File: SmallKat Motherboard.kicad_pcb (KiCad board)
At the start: 2 copper layers, 100 x 56 mm, 145 parts, among them IC1 LMR14010A, IC2 LMR14010A, IC3 TPS40192DRCT-TPS40192DRCT, IC4 ESP32-S3-MINI-1-N8, J1 BATT_SERIAL, J10 Conn_01x03_Male, J11 Conn_01x03_Male, J12 Conn_01x03_Male, J13 Conn_01x03_Male, J14 Conn_01x03_Male, J15 Conn_01x03_Male, J16 Conn_01x03_Male, J17 Conn_01x03_Male, J18 Conn_01x03_Male, J19 Conn_01x03_Male, J2 BATT_SERIAL, J20 Conn_01x03_Male, J21 Conn_01x03_Male, J22 Conn_01x03_Male, J23 Conn_01x03_Male, J24 Conn_01x03_Male, J25 Conn_01x02_Female, J3 Conn_01x03_Male, J4 Conn_01x03_Male, J5 Conn_01x03_Male, J6 Conn_01x03_Male, J8 USB_C_Receptacle, J9 Conn_01x03_Male, Q2 AON7262E, Q3 AON7262E, SW1 SW_SPST, SW2 SW_SPST, Y1 32.768kHz

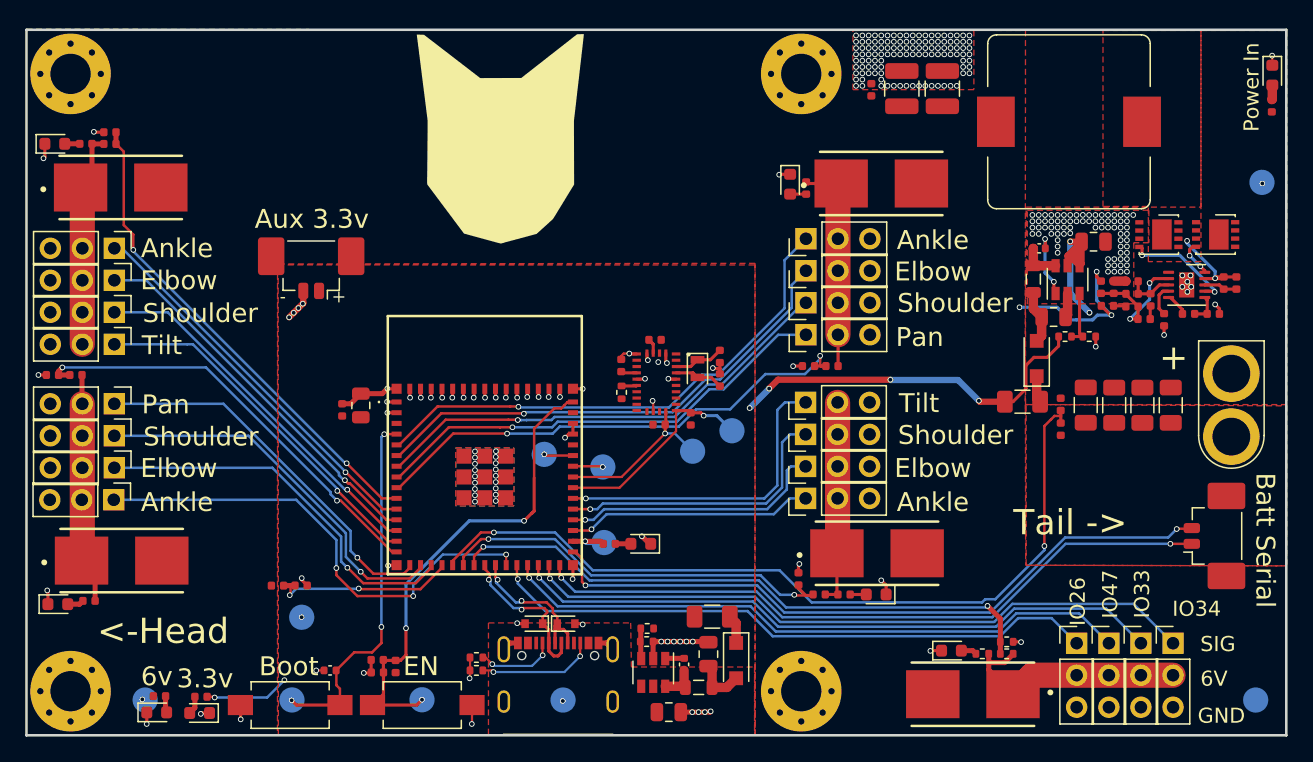
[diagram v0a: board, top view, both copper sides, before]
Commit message: Adding usb c pd negotiation for battery charging
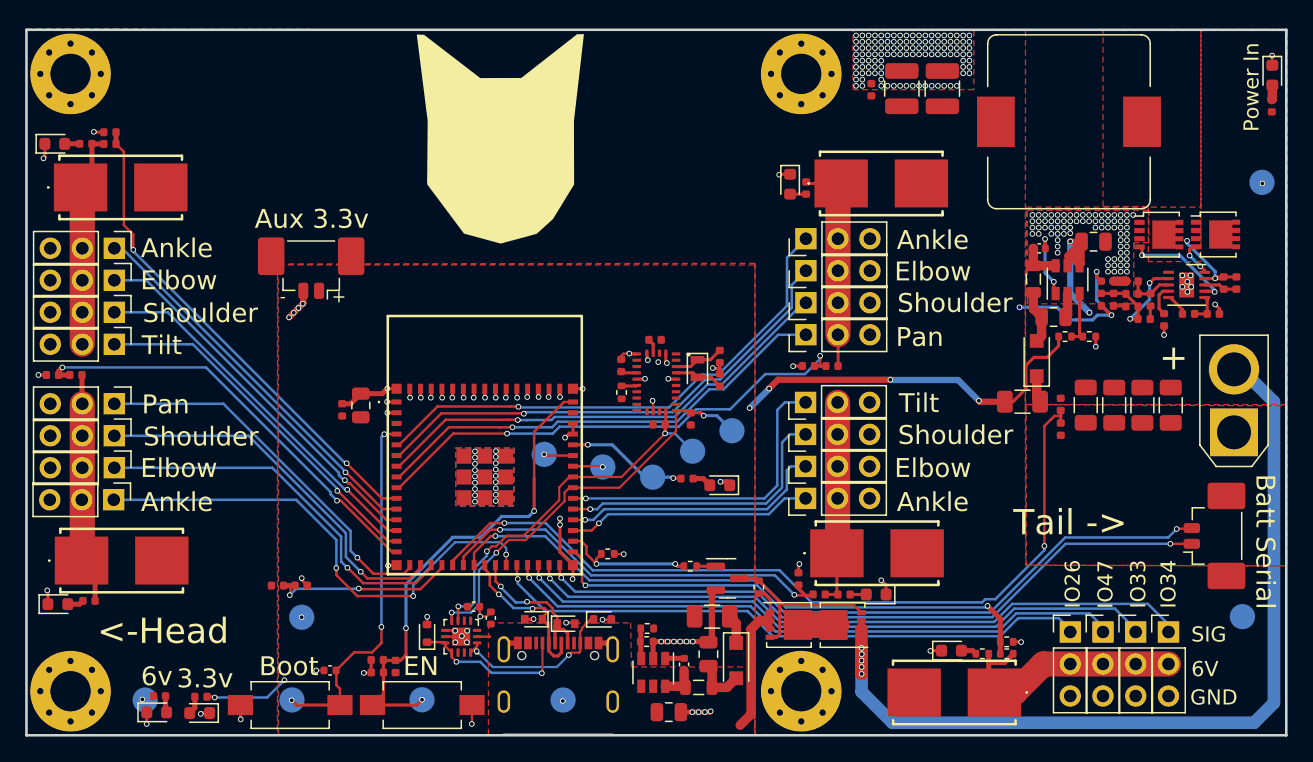
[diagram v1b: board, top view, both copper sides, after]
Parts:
- removed R14, R18: 5.1K, Resistor_SMD:R_0402_1005Metric
- added C7: 0.1μF, Capacitor_SMD:C_0402_1005Metric, F.Cu at (103.6, 127.6)
- added C8: 1μF, Capacitor_SMD:C_0402_1005Metric, F.Cu at (105.0, 128.5)
- added D14: D_TVS, Diode_SMD:D_SOD-523, F.Cu at (100.0, 129.7)
- added D17: D_TVS, Diode_SMD:D_SOD-523, F.Cu at (113.9, 128.6)
- added Q1: MMBT3904, Package_TO_SOT_SMD:SOT-23, F.Cu at (123.8, 125.3)
- added Q4: DMP3017SFG, Package_SON:Diodes_PowerDI3333-8, F.Cu at (128.7, 129.0)
- added Q5: DMP3017SFG, Package_SON:Diodes_PowerDI3333-8, F.Cu at (132.9, 129.0)
- added R21: 10kΩ, Resistor_SMD:R_0402_1005Metric, F.Cu at (114.3, 123.4)
- added R22: 2kΩ, Resistor_SMD:R_0402_1005Metric, F.Cu at (120.8, 124.4)
- added R44: 100kΩ, Resistor_SMD:R_0402_1005Metric, F.Cu at (126.3, 126.0)
- added U1: FUSB302BMPX, Package_DFN_QFN:WQFN-14-1EP_2.5x2.5mm_P0.5mm_EP1.45x1.45mm, F.Cu at (102.7, 130.0)
- F1, F2, F3, F4, F5: footprint 01550900M:0154.250DR -> 0155.500:0154500DRTL
- IC4: footprint ESP32-s3-wroom-mini:ESP32S3MINI1N8 -> ESP32-S3-MINI:ESP32S3MINI1N8
- J25: footprint RC-Battery-Connectors:XT-60_male -> Connector_AMASS:AMASS_XT30U-F_1x02_P5.0mm_Vertical
- Q2, Q3: footprint 2450AT43F0100:DFN-8 -> Package_TO_SOT_SMD:LFPAK33
- moved REF** 65.5 mm to (87.8, 87.3)
- moved REF** 65.5 mm to (87.8, 94.8)
- moved R1 8.06 mm to (120.6, 117.4)
- moved D1 7.81 mm to (123.2, 118.0)
- moved TP10 6.70 mm to (164.7, 128.4)
- moved TP1 6.47 mm to (117.9, 117.3)
- moved J25 2.17 mm to (164.0, 113.8), turned to 90 degrees
- moved F1 1.48 mm to (141.8, 134.4)
- moved J3 1.03 mm to (151.0, 129.6)
- moved J5 1.01 mm to (153.6, 129.6)
- moved J4 0.98 mm to (156.2, 129.6)
- moved J6 0.96 mm to (158.8, 129.6)
- moved D7 0.35 mm to (108.4, 128.6)
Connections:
- net /MainBoard/ESP32Module/USBD_N renamed /MainBoard/USB_N
- net /MainBoard/ESP32Module/USBD_P renamed /MainBoard/USB_P
- IC4 pad 32: /MainBoard/ESP32Module/IO36 -> /MainBoard/OUT_CTRL
- J25 pad 1: +BATT -> GND
- J25 pad 2: GND -> +BATT
- J8 pad A5: Net-(J8-PadA5) -> /MainBoard/USB_PD/CC1
- J8 pad B5: Net-(J8-PadB5) -> /MainBoard/USB_PD/CC2
- R1 pad 1: /MainBoard/ESP32Module/IO36 -> /MainBoard/ESP32Module/IO45
- TP1 pad 1: /MainBoard/ESP32Module/IO36 -> /MainBoard/ESP32Module/IO45
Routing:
- net +BATT: track 16.9 -> 87.2 mm, vias 3 -> 8
- net /MainBoard/SCL: track 13.3 -> 30.2 mm, vias 1 -> 3
- net /MainBoard/SDA: track 16.9 -> 33.3 mm, vias 1 -> 3
- net VBUS: track 0.00 -> 16.1 mm
- net Net-(Q1-C): track 0.00 -> 14.3 mm
- net /MainBoard/USB_PD/CC2: track 0.00 -> 13.8 mm, vias 0 -> 2
- net GND: track 67.3 -> 80.9 mm, vias 283 -> 293
- net /MainBoard/USB_PD/CC1: track 0.00 -> 12.9 mm, vias 0 -> 2
- net /MainBoard/OUT_CTRL: track 0.00 -> 10.9 mm, vias 0 -> 2
- net Net-(J8-PadB5): track 9.35 -> 0.00 mm, vias 2 -> 0
- net /MainBoard/ESP32Module/IO45: track 0.00 -> 9.04 mm, vias 0 -> 2
- net Net-(J8-PadA5): track 6.36 -> 0.00 mm, vias 2 -> 0
- net Net-(Q4-D): track 0.00 -> 4.66 mm
- net /MainBoard/ESP32Module/IO36: track 4.02 -> 0.00 mm, vias 1 -> 0
- net Net-(Q1-B): track 0.00 -> 1.52 mm
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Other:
- board text added: "IO 45"
- board text removed: "IO 36"
